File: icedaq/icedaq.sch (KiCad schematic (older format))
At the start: 14 parts, among them P1 UART, U1 REG12, U2 iCE40HX1K-VQ100, U3 RPi

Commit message: icedaq: update
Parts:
- added unit 3 of U2
- added unit 6 of U2
- CR1, CR2: footprint (none) -> Capacitors_SMD:C_0603_HandSoldering
- D2_5: footprint (none) -> local:D_0603_HandSoldering
- P1: footprint (none) -> Pin_Headers:Pin_Header_Straight_1x04
- R121, R122, R123, RDN1, RRST1, RSCK1, RSS1: footprint (none) -> Resistors_SMD:R_0603_HandSoldering
- U1: footprint (none) -> local:SOT23-5
- U2: footprint (none) -> local:VQFP-100
- U3: footprint (none) -> Pin_Headers:Pin_Header_Straight_2x20
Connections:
- wire segments 53 -> 57
- no-connect marks 14 -> 55
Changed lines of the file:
@@
 LIBS:rpi
 LIBS:adc082s021
+LIBS:dacx311
 LIBS:icedaq-cache
 EELAYER 25 0
@@
 F 0 "U1" H 9050 1700 60  0000 C CNN
 F 1 "REG12" H 8850 1350 60  0001 C CNN
-F 2 "" H 8850 1450 60  0000 C CNN
+F 2 "local:SOT23-5" H 8850 1450 60  0001 C CNN
 F 3 "" H 8850 1450 60  0000 C CNN
 	1    8850 1400
@@
 F 0 "CR1" H 8200 1350 50  0000 L CNN
 F 1 "1u" H 8110 1270 50  0000 L CNN
-F 2 "" H 8100 1350 50  0000 C CNN
+F 2 "Capacitors_SMD:C_0603_HandSoldering" H 8100 1350 50  0001 C CNN
 F 3 "" H 8100 1350 50  0000 C CNN
 	1    8100 1350
@@
 F 0 "CR2" H 10100 1350 50  0000 L CNN
 F 1 "1u" H 10010 1270 50  0000 L CNN
-F 2 "" H 10000 1350 50  0000 C CNN
+F 2 "Capacitors_SMD:C_0603_HandSoldering" H 10000 1350 50  0001 C CNN
 F 3 "" H 10000 1350 50  0000 C CNN
 	1    10000 1350
@@
 F 0 "R121" V 9580 1400 50  0000 C CNN
 F 1 "10k" V 9500 1400 50  0000 C CNN
-F 2 "" V 9430 1400 50  0000 C CNN
+F 2 "Resistors_SMD:R_0603_HandSoldering" V 9430 1400 50  0001 C CNN
 F 3 "" H 9500 1400 50  0000 C CNN
 	1    9500 1400
@@
 F 0 "R122" V 9830 1400 50  0000 C CNN
 F 1 "10k" V 9750 1400 50  0000 C CNN
-F 2 "" V 9680 1400 50  0000 C CNN
+F 2 "Resistors_SMD:R_0603_HandSoldering" V 9680 1400 50  0001 C CNN
 F 3 "" H 9750 1400 50  0000 C CNN
 	1    9750 1400
@@
 F 0 "R123" V 9830 1850 50  0000 C CNN
 F 1 "10k" V 9750 1850 50  0000 C CNN
-F 2 "" V 9680 1850 50  0000 C CNN
+F 2 "Resistors_SMD:R_0603_HandSoldering" V 9680 1850 50  0001 C CNN
 F 3 "" H 9750 1850 50  0000 C CNN
 	1    9750 1850
@@
 F 0 "U2" H 5900 2000 60  0000 C CNN
 F 1 "iCE40HX1K-VQ100" H 5850 2200 60  0001 C CNN
-F 2 "" H 6100 1500 60  0000 C CNN
+F 2 "local:VQFP-100" H 6100 1500 60  0001 C CNN
 F 3 "" H 6100 1500 60  0000 C CNN
 	1    5850 1400
@@
 F 0 "D2_5" H 6700 1730 50  0000 L CNN
 F 1 "D_Schottky_Small" H 6470 1570 50  0001 L CNN
-F 2 "" V 6750 1650 50  0000 C CNN
+F 2 "local:D_0603_HandSoldering" V 6750 1650 50  0001 C CNN
 F 3 "" V 6750 1650 50  0000 C CNN
 	1    6750 1650
@@
 F 0 "U2" H 3300 1650 60  0000 C CNN
 F 1 "iCE40HX1K-VQ100" H 3150 2150 60  0001 C CNN
-F 2 "" H 3400 1450 60  0000 C CNN
+F 2 "local:VQFP-100" H 3400 1450 60  0001 C CNN
 F 3 "" H 3400 1450 60  0000 C CNN
 	2    3150 1350
@@
 F 0 "RDN1" H 4350 1800 50  0000 C CNN
 F 1 "10k" V 4200 1800 50  0000 C CNN
-F 2 "" V 4130 1800 50  0000 C CNN
+F 2 "Resistors_SMD:R_0603_HandSoldering" V 4130 1800 50  0001 C CNN
 F 3 "" H 4200 1800 50  0000 C CNN
 	1    4200 1800
@@
 F 0 "RRST1" H 4000 1900 50  0000 C CNN
 F 1 "10k" V 3850 1900 50  0000 C CNN
-F 2 "" V 3780 1900 50  0000 C CNN
+F 2 "Resistors_SMD:R_0603_HandSoldering" V 3780 1900 50  0001 C CNN
 F 3 "" H 3850 1900 50  0000 C CNN
 	1    3850 1900
@@
 F 0 "RSCK1" H 4200 1300 50  0000 C CNN
 F 1 "10k" V 4000 1300 50  0000 C CNN
-F 2 "" V 3930 1300 50  0000 C CNN
+F 2 "Resistors_SMD:R_0603_HandSoldering" V 3930 1300 50  0001 C CNN
 F 3 "" H 4000 1300 50  0000 C CNN
 	1    4000 1300
@@
 F 0 "RSS1" H 4600 1400 50  0000 C CNN
 F 1 "10k" V 4400 1400 50  0000 C CNN
-F 2 "" V 4330 1400 50  0000 C CNN
+F 2 "Resistors_SMD:R_0603_HandSoldering" V 4330 1400 50  0001 C CNN
 F 3 "" H 4400 1400 50  0000 C CNN
 	1    4400 1400
@@
 F 0 "U3" H 9500 5800 60  0000 C CNN
 F 1 "RPi" H 8950 5050 60  0000 C CNN
-F 2 "" H 8750 4500 60  0000 C CNN
+F 2 "Pin_Headers:Pin_Header_Straight_2x20" H 8750 4500 60  0001 C CNN
 F 3 "" H 8750 4500 60  0000 C CNN
 	1    8750 4500
@@
 F 0 "P1" H 8800 3000 50  0000 C CNN
 F 1 "UART" V 8900 2750 50  0000 C CNN
-F 2 "" H 8800 2750 50  0000 C CNN
+F 2 "Pin_Headers:Pin_Header_Straight_1x04" H 8800 2750 50  0001 C CNN
 F 3 "" H 8800 2750 50  0000 C CNN
 	1    8800 2750
@@
 	3600 1350 3850 1350
 Wire Wire Line
-	3600 1450 4000 1450
-Wire Wire Line
-	3600 1550 4400 1550
-Wire Wire Line
-	3600 1650 4200 1650
-Wire Wire Line
-	3600 1750 3850 1750
+	3600 1450 4100 1450
+Wire Wire Line
+	3600 1550 4500 1550
+Wire Wire Line
+	3600 1650 4300 1650
+Wire Wire Line
+	3600 1750 3950 1750
 Wire Wire Line
 	9800 3650 9800 3750
@@
 F 0 "U2" H 5550 5300 60  0000 C CNN
 F 1 "iCE40HX1K-VQ100" H 5100 5500 60  0001 C CNN
-F 2 "" H 5350 4800 60  0000 C CNN
+F 2 "local:VQFP-100" H 5350 4800 60  0001 C CNN
 F 3 "" H 5350 4800 60  0000 C CNN
 	5    5100 4700
@@
 	4400 4900 4100 4900
 $Comp
-L +3.3V #PWR?
+L +3.3V #PWR025
 U 1 1 58615E10
 P 5450 5300
-F 0 "#PWR?" H 5450 5150 50  0001 C CNN
+F 0 "#PWR025" H 5450 5150 50  0001 C CNN
 F 1 "+3.3V" H 5450 5440 50  0000 C CNN
 F 2 "" H 5450 5300 50  0000 C CNN
@@
 Connection ~ 5350 5300
 $Sheet
-S 1200 3300 1200 1250
+S 1000 1100 1200 1250
 U 58616DAE
 F0 "Analog" 60
 F1 "icedaq-analog.sch" 60
 $EndSheet
+NoConn ~ 5750 4700
+NoConn ~ 4400 4700
+NoConn ~ 4400 4600
+NoConn ~ 4400 4500
+NoConn ~ 4400 4400
+$Comp
+L iCE40HX1K-VQ100 U2
+U 3 1 59912301
+P 2300 6350
+F 0 "U2" H 2750 6950 60  0000 C CNN
+F 1 "iCE40HX1K-VQ100" H 2300 7150 60  0001 C CNN
+F 2 "local:VQFP-100" H 2550 6450 60  0001 C CNN
+F 3 "" H 2550 6450 60  0000 C CNN
+	3    2300 6350
+	1    0    0    -1
+$EndComp
+$Comp
+L iCE40HX1K-VQ100 U2
+U 6 1 599123FB
+P 4350 6400
+F 0 "U2" H 4800 7000 60  0000 C CNN
+F 1 "iCE40HX1K-VQ100" H 4350 7200 60  0001 C CNN
+F 2 "local:VQFP-100" H 4600 6500 60  0001 C CNN
+F 3 "" H 4600 6500 60  0000 C CNN
+	6    4350 6400
+	1    0    0    -1
+$EndComp
+Connection ~ 4000 1450
+Connection ~ 4400 1550
+Connection ~ 4200 1650
+Connection ~ 3850 1750
+NoConn ~ 5300 6000
+NoConn ~ 5300 6100
+NoConn ~ 5300 6200
+NoConn ~ 5300 6300
+NoConn ~ 5300 6400
+NoConn ~ 5300 6500
+NoConn ~ 5300 6600
+NoConn ~ 5300 6700
+NoConn ~ 3600 6900
+NoConn ~ 3600 6800
+NoConn ~ 3600 6700
+NoConn ~ 3600 6600
+NoConn ~ 3600 6500
+NoConn ~ 3600 6400
+NoConn ~ 3600 6300
+NoConn ~ 3600 6200
+NoConn ~ 3600 6100
+NoConn ~ 3600 6000
+NoConn ~ 3050 6850
+NoConn ~ 3050 6750
+NoConn ~ 3050 6650
+NoConn ~ 3050 6550
+NoConn ~ 3050 6450
+NoConn ~ 3050 6350
+NoConn ~ 3050 6250
+NoConn ~ 3050 6150
+NoConn ~ 3050 6050
+NoConn ~ 1600 6050
+NoConn ~ 1600 6150
+NoConn ~ 1600 6250
+NoConn ~ 1600 6350
+NoConn ~ 1600 6450
+NoConn ~ 1600 6550
+NoConn ~ 1600 6650
+NoConn ~ 1600 6750
+NoConn ~ 1600 6850
+Wire Wire Line
+	2350 7200 2450 7200
+Wire Wire Line
+	2450 7200 2450 7250
+Wire Wire Line
+	4600 7300 4700 7300
+Wire Wire Line
+	4700 7300 4700 7350
+$Comp
+L +3.3V #PWR026
+U 1 1 59914C50
+P 4700 7350
+F 0 "#PWR026" H 4700 7200 50  0001 C CNN
+F 1 "+3.3V" H 4700 7490 50  0000 C CNN
+F 2 "" H 4700 7350 50  0000 C CNN
+F 3 "" H 4700 7350 50  0000 C CNN
+	1    4700 7350
+	-1   0    0    1
+$EndComp
+$Comp
+L +3.3V #PWR027
+U 1 1 59914C91
+P 2450 7250
+F 0 "#PWR027" H 2450 7100 50  0001 C CNN
+F 1 "+3.3V" H 2450 7390 50  0000 C CNN
+F 2 "" H 2450 7250 50  0000 C CNN
+F 3 "" H 2450 7250 50  0000 C CNN
+	1    2450 7250
+	-1   0    0    1
+$EndComp
 $EndSCHEMATC

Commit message: icedaq layout
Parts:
- removed unit 3 of U2
- added CD1, CD3, CD4, CD5: C_Small, Capacitors_SMD:C_0603_HandSoldering, symbol C_Small
- added R1: 10k, Resistors_SMD:R_0603_HandSoldering, symbol R
- added RB1, RB2: 3.9k, Resistors_SMD:R_0603_HandSoldering, symbol R
- added ROM1: CAT24C, Housings_SOIC:SOIC-8_3.9x4.9mm_Pitch1.27mm, symbol 24LC32
- added U4: oscillator4, local:OSC_SMD_1, symbol oscillator4
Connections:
- net labels added: ID_SC, ID_SD, clk
- wire segments 57 -> 67
- no-connect marks 55 -> 37
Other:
- note added: "Break out MCU UART"
- note added: "See https://github.com/raspberrypi/hats/blob/master/designguide.md"
- note added: "UART"
- note added: "Write protect\nflows low (disabled)"
- note removed: "UART to\nheader"
- moved on the sheet: P1

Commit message: icedaq more
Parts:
- added P2: GPIO, Pin_Headers:Pin_Header_Straight_1x05_Pitch2.00mm, symbol CONN_01X05
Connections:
- wire segments 67 -> 71
- no-connect marks 37 -> 33
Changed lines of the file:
@@
 NoConn ~ 5300 6200
 NoConn ~ 5300 6300
-NoConn ~ 5300 6400
-NoConn ~ 5300 6500
-NoConn ~ 5300 6600
-NoConn ~ 5300 6700
 NoConn ~ 3600 6800
 NoConn ~ 3600 6700
@@
 $EndComp
 $Comp
-L GND #PWR031
+L GND #PWR029
 U 1 1 599273C4
 P 4150 3100
-F 0 "#PWR031" H 4150 2850 50  0001 C CNN
+F 0 "#PWR029" H 4150 2850 50  0001 C CNN
 F 1 "GND" H 4150 2950 50  0000 C CNN
 F 2 "" H 4150 3100 50  0000 C CNN
@@
 $EndComp
 $Comp
-L +3.3V #PWR032
+L +3.3V #PWR030
 U 1 1 599273CA
 P 4150 2900
-F 0 "#PWR032" H 4150 2750 50  0001 C CNN
+F 0 "#PWR030" H 4150 2750 50  0001 C CNN
 F 1 "+3.3V" H 4150 3040 50  0000 C CNN
 F 2 "" H 4150 2900 50  0000 C CNN
@@
 $EndComp
 $Comp
-L GND #PWR033
+L GND #PWR031
 U 1 1 599274AA
 P 3400 3100
-F 0 "#PWR033" H 3400 2850 50  0001 C CNN
+F 0 "#PWR031" H 3400 2850 50  0001 C CNN
 F 1 "GND" H 3400 2950 50  0000 C CNN
 F 2 "" H 3400 3100 50  0000 C CNN
@@
 $EndComp
 $Comp
-L +3.3V #PWR034
+L +3.3V #PWR032
 U 1 1 599274B0
 P 3400 2900
-F 0 "#PWR034" H 3400 2750 50  0001 C CNN
+F 0 "#PWR032" H 3400 2750 50  0001 C CNN
 F 1 "+3.3V" H 3400 3040 50  0000 C CNN
 F 2 "" H 3400 2900 50  0000 C CNN
@@
 $EndComp
 $Comp
-L GND #PWR035
+L GND #PWR033
 U 1 1 59927E27
 P 6400 2850
-F 0 "#PWR035" H 6400 2600 50  0001 C CNN
+F 0 "#PWR033" H 6400 2600 50  0001 C CNN
 F 1 "GND" H 6400 2700 50  0000 C CNN
 F 2 "" H 6400 2850 50  0000 C CNN
@@
 $EndComp
 $Comp
-L +1V2 #PWR036
+L +1V2 #PWR034
 U 1 1 59927E92
 P 6400 2650
-F 0 "#PWR036" H 6400 2500 50  0001 C CNN
+F 0 "#PWR034" H 6400 2500 50  0001 C CNN
 F 1 "+1V2" H 6400 2790 50  0000 C CNN
 F 2 "" H 6400 2650 50  0000 C CNN
@@
 $EndComp
 $Comp
-L GND #PWR037
+L GND #PWR035
 U 1 1 59927F5C
 P 6650 2850
-F 0 "#PWR037" H 6650 2600 50  0001 C CNN
+F 0 "#PWR035" H 6650 2600 50  0001 C CNN
 F 1 "GND" H 6650 2700 50  0000 C CNN
 F 2 "" H 6650 2850 50  0000 C CNN
@@
 $EndComp
 $Comp
-L +1V2 #PWR038
+L +1V2 #PWR036
 U 1 1 59927F62
 P 6650 2650
-F 0 "#PWR038" H 6650 2500 50  0001 C CNN
+F 0 "#PWR036" H 6650 2500 50  0001 C CNN
 F 1 "+1V2" H 6650 2790 50  0000 C CNN
 F 2 "" H 6650 2650 50  0000 C CNN
@@
 F 1 "CAT24C" H 1750 6550 50  0000 C CNN
 F 2 "Housings_SOIC:SOIC-8_3.9x4.9mm_Pitch1.27mm" H 1600 6050 50  0001 L CNN
-F 3 "" H 1550 6200 50  0000 C CNN
+F 3 "http://www.onsemi.com/pub/Collateral/CAT24C32-D.PDF" H 1550 6200 50  0001 C CNN
 	1    1550 6300
 	1    0    0    -1
 $EndComp
 $Comp
-L GND #PWR039
+L GND #PWR037
 U 1 1 5992C4A3
 P 1550 6600
-F 0 "#PWR039" H 1550 6350 50  0001 C CNN
+F 0 "#PWR037" H 1550 6350 50  0001 C CNN
 F 1 "GND" H 1550 6450 50  0000 C CNN
 F 2 "" H 1550 6600 50  0000 C CNN
@@
 Connection ~ 1150 6400
 $Comp
-L GND #PWR040
+L GND #PWR038
 U 1 1 5992C6A3
 P 1150 6550
-F 0 "#PWR040" H 1150 6300 50  0001 C CNN
+F 0 "#PWR038" H 1150 6300 50  0001 C CNN
 F 1 "GND" H 1150 6400 50  0000 C CNN
 F 2 "" H 1150 6550 50  0000 C CNN
@@
 $EndComp
 $Comp
-L +3.3V #PWR041
+L +3.3V #PWR039
 U 1 1 5992C712
 P 1550 6000
-F 0 "#PWR041" H 1550 5850 50  0001 C CNN
+F 0 "#PWR039" H 1550 5850 50  0001 C CNN
 F 1 "+3.3V" H 1550 6140 50  0000 C CNN
 F 2 "" H 1550 6000 50  0000 C CNN
@@
 $EndComp
 $Comp
-L +3.3V #PWR042
+L +3.3V #PWR040
 U 1 1 5992D326
 P 2200 5750
-F 0 "#PWR042" H 2200 5600 50  0001 C CNN
+F 0 "#PWR040" H 2200 5600 50  0001 C CNN
 F 1 "+3.3V" H 2200 5890 50  0000 C CNN
 F 2 "" H 2200 5750 50  0000 C CNN
@@
 $EndComp
 $Comp
-L +3.3V #PWR043
+L +3.3V #PWR041
 U 1 1 5992D39D
 P 2450 5750
-F 0 "#PWR043" H 2450 5600 50  0001 C CNN
+F 0 "#PWR041" H 2450 5600 50  0001 C CNN
 F 1 "+3.3V" H 2450 5890 50  0000 C CNN
 F 2 "" H 2450 5750 50  0000 C CNN
@@
 	9800 3500 9950 3500
 NoConn ~ 1950 6400
+$Comp
+L CONN_01X05 P2
+U 1 1 59932164
+P 5700 6600
+F 0 "P2" H 5700 6900 50  0000 C CNN
+F 1 "GPIO" V 5800 6600 50  0000 C CNN
+F 2 "Pin_Headers:Pin_Header_Straight_1x05_Pitch2.00mm" H 5700 6600 50  0001 C CNN
+F 3 "" H 5700 6600 50  0000 C CNN
+	1    5700 6600
+	1    0    0    -1
+$EndComp
+Wire Wire Line
+	5500 6400 5300 6400
+Wire Wire Line
+	5300 6500 5500 6500
+Wire Wire Line
+	5500 6600 5300 6600
+Wire Wire Line
+	5300 6700 5500 6700
+$Comp
+L GND #PWR042
+U 1 1 599324BC
+P 5500 6800
+F 0 "#PWR042" H 5500 6550 50  0001 C CNN
+F 1 "GND" H 5500 6650 50  0000 C CNN
+F 2 "" H 5500 6800 50  0000 C CNN
+F 3 "" H 5500 6800 50  0000 C CNN
+	1    5500 6800
+	1    0    0    -1
+$EndComp
 $EndSCHEMATC

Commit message: minor
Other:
- note added: "Identification EEPROM"
- note added: "iCE40 configure control\n(GPIO)"
- note removed: "iCE40 configure control"
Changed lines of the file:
@@
 SPI1 for debug
 Text Notes 7400 5650 2    60   ~ 0
-iCE40 configure control
+iCE40 configure control\n(GPIO)
 Text Notes 7350 4650 2    60   ~ 0
 UART
@@
 	1    0    0    -1
 $EndComp
+Text Notes 800  5650 0    60   ~ 0
+Identification EEPROM
 $EndSCHEMATC

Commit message: icedaq: update
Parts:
- added TP1: WP, local:testpoint, symbol TEST
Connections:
- net labels removed: GCLK2
- wire segments 71 -> 66
- no-connect marks 33 -> 37
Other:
- note added: "SPI0 for application"
- note added: "SPI1 for configure/debug"
- note added: "https://github.com/raspberrypi/hats/blob/master/designguide.md"
- note removed: "SPI0 to configure"
- note removed: "SPI1 for debug"
- note removed: "See https://github.com/raspberrypi/hats/blob/master/designguide.md"
- moved on the sheet: P2
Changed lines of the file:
@@
 Title "iCE40 Raspberry Pi 3b GPIO"
 Date ""
-Rev "1"
+Rev "draft"
 Comp "MAD"
 Comment1 ""
@@
 	1    0    0    -1
 $EndComp
-Text Label 7800 4100 2    60   ~ 0
+Text Label 7800 5100 2    60   ~ 0
 MISO
-Text Label 7800 4200 2    60   ~ 0
+Text Label 7800 5200 2    60   ~ 0
 MOSI
-Text Label 7800 4300 2    60   ~ 0
+Text Label 7800 5300 2    60   ~ 0
 SCK
-Text Label 7750 4000 2    60   ~ 0
+Text Label 7750 4800 2    60   ~ 0
 SS
 Text Label 7800 5600 2    60   ~ 0
@@
 NoConn ~ 7850 5400
 NoConn ~ 7850 4900
-NoConn ~ 7850 4800
+NoConn ~ 7850 5000
 NoConn ~ 7850 3900
 NoConn ~ 7850 3500
@@
 Text Label 7800 4700 2    60   ~ 0
 RXD
-Text Label 7800 5000 2    60   ~ 0
-SS1
-Text Label 7800 5100 2    60   ~ 0
-MISO1
-Text Label 7800 5200 2    60   ~ 0
-MOSI1
-Text Label 7800 5300 2    60   ~ 0
-SCLK1
-Text Notes 7350 4150 2    60   ~ 0
-SPI0 to configure
+Text Notes 7100 4150 2    60   ~ 0
+SPI0 for application
 Text Notes 7350 5150 2    60   ~ 0
-SPI1 for debug
+SPI1 for configure/debug
 Text Notes 7400 5650 2    60   ~ 0
 iCE40 configure control\n(GPIO)
@@
 Connection ~ 9800 4250
 Wire Wire Line
-	7850 4100 7600 4100
-Wire Wire Line
-	7850 4200 7600 4200
-Wire Wire Line
-	7850 4300 7600 4300
-Wire Wire Line
-	7850 4000 7600 4000
+	7850 5100 7600 5100
+Wire Wire Line
+	7850 5200 7600 5200
+Wire Wire Line
+	7850 5300 7600 5300
+Wire Wire Line
+	7850 4800 7600 4800
 Wire Wire Line
 	7850 5700 7600 5700
@@
 Connection ~ 6550 1650
 Wire Wire Line
-	7850 3600 7650 3600
-Wire Wire Line
 	7850 3700 7650 3700
 Wire Wire Line
@@
 	7850 4700 7600 4700
 Wire Wire Line
-	7850 5000 7600 5000
-Wire Wire Line
-	7850 5100 7600 5100
-Wire Wire Line
-	7850 5200 7600 5200
-Wire Wire Line
-	7850 5300 7600 5300
+	7850 4000 7750 4000
+Wire Wire Line
+	7850 4100 7450 4100
+Wire Wire Line
+	7850 4200 7800 4200
+Wire Wire Line
+	7850 4300 7450 4300
 Wire Wire Line
 	6900 6100 6650 6100
@@
 Text Label 4300 5000 2    60   ~ 0
 GCLK1
-Wire Wire Line
-	5750 4300 6050 4300
-Wire Wire Line
-	5750 4400 6050 4400
-Wire Wire Line
-	5750 4500 6050 4500
-Wire Wire Line
-	5750 4600 6050 4600
-Text Label 5850 4300 0    60   ~ 0
-SS1
-Text Label 5800 4600 0    60   ~ 0
-MISO1
-Text Label 5800 4500 0    60   ~ 0
-MOSI1
-Text Label 5800 4400 0    60   ~ 0
-SCLK1
 Wire Wire Line
 	4400 4900 4100 4900
@@
 NoConn ~ 5300 6300
 NoConn ~ 3600 6800
-NoConn ~ 3600 6700
-NoConn ~ 3600 6600
-NoConn ~ 3600 6500
-NoConn ~ 3600 6400
 NoConn ~ 3600 6300
 NoConn ~ 3600 6200
@@
 	1    0    0    -1
 $EndComp
-Text GLabel 2950 4000 2    60   Input ~ 0
+Text GLabel 2950 4000 2    60   Output ~ 0
 clk
 $Comp
@@
 $EndComp
 NoConn ~ 4400 4800
-Text GLabel 7650 3550 1    60   Input ~ 0
-GCLK2
-Wire Wire Line
-	7650 3600 7650 3550
-Text Notes 6350 6900 0    60   ~ 0
-See https://github.com/raspberrypi/hats/blob/master/designguide.md
+Text Notes 7200 3050 0    60   ~ 0
+https://github.com/raspberrypi/hats/blob/master/designguide.md
 Text Notes 7300 6450 0    60   ~ 0
 Break out MCU UART
@@
 	1    0    0    -1
 $EndComp
-Text Notes 1800 6850 0    60   ~ 0
+Text Notes 1700 7150 0    60   ~ 0
 Write protect\nflows low (disabled)
 $Comp
@@
 Wire Wire Line
 	9800 3500 9950 3500
-NoConn ~ 1950 6400
 $Comp
 L CONN_01X05 P2
 U 1 1 59932164
-P 5700 6600
-F 0 "P2" H 5700 6900 50  0000 C CNN
-F 1 "GPIO" V 5800 6600 50  0000 C CNN
-F 2 "Pin_Headers:Pin_Header_Straight_1x05_Pitch2.00mm" H 5700 6600 50  0001 C CNN
-F 3 "" H 5700 6600 50  0000 C CNN
-	1    5700 6600
-	1    0    0    -1
-$EndComp
-Wire Wire Line
-	5500 6400 5300 6400
-Wire Wire Line
-	5300 6500 5500 6500
-Wire Wire Line
-	5500 6600 5300 6600
-Wire Wire Line
-	5300 6700 5500 6700
+P 3200 6600
+F 0 "P2" H 3200 6900 50  0000 C CNN
+F 1 "GPIO" V 3300 6600 50  0000 C CNN
+F 2 "Pin_Headers:Pin_Header_Straight_1x05_Pitch2.00mm" H 3200 6600 50  0001 C CNN
+F 3 "" H 3200 6600 50  0000 C CNN
+	1    3200 6600
+	-1   0    0    -1
+$EndComp
+Wire Wire Line
+	3400 6400 3600 6400
+Wire Wire Line
+	3600 6500 3400 6500
+Wire Wire Line
+	3400 6600 3600 6600
+Wire Wire Line
+	3600 6700 3400 6700
 $Comp
 L GND #PWR042
 U 1 1 599324BC
-P 5500 6800
-F 0 "#PWR042" H 5500 6550 50  0001 C CNN
-F 1 "GND" H 5500 6650 50  0000 C CNN
-F 2 "" H 5500 6800 50  0000 C CNN
-F 3 "" H 5500 6800 50  0000 C CNN
-	1    5500 6800
-	1    0    0    -1
+P 3400 6800
+F 0 "#PWR042" H 3400 6550 50  0001 C CNN
+F 1 "GND" H 3400 6650 50  0000 C CNN
+F 2 "" H 3400 6800 50  0000 C CNN
+F 3 "" H 3400 6800 50  0000 C CNN
+	1    3400 6800
+	-1   0    0    -1
 $EndComp
 Text Notes 800  5650 0    60   ~ 0
 Identification EEPROM
+Text GLabel 7750 4000 0    60   Output ~ 0
+SS1
+Text GLabel 7450 4100 0    60   Input ~ 0
+MISO1
+Text GLabel 7800 4200 0    60   Output ~ 0
+MOSI1
+Text GLabel 7450 4300 0    60   Output ~ 0
+SCLK1
+NoConn ~ 5750 4300
+NoConn ~ 5750 4400
+NoConn ~ 5750 4500
+NoConn ~ 5750 4600
+NoConn ~ 5300 6400
+NoConn ~ 5300 6500
+NoConn ~ 5300 6600
+NoConn ~ 5300 6700
+NoConn ~ 7850 3600
+$Comp
+L TEST TP1
+U 1 1 599CB445
+P 2100 6400
+F 0 "TP1" H 2100 6700 50  0000 C BNN
+F 1 "WP" H 2100 6650 50  0000 C CNN
+F 2 "local:testpoint" H 2100 6400 50  0001 C CNN
+F 3 "" H 2100 6400 50  0000 C CNN
+	1    2100 6400
+	-1   0    0    1
+$EndComp
+Wire Wire Line
+	2100 6400 1950 6400
 $EndSCHEMATC

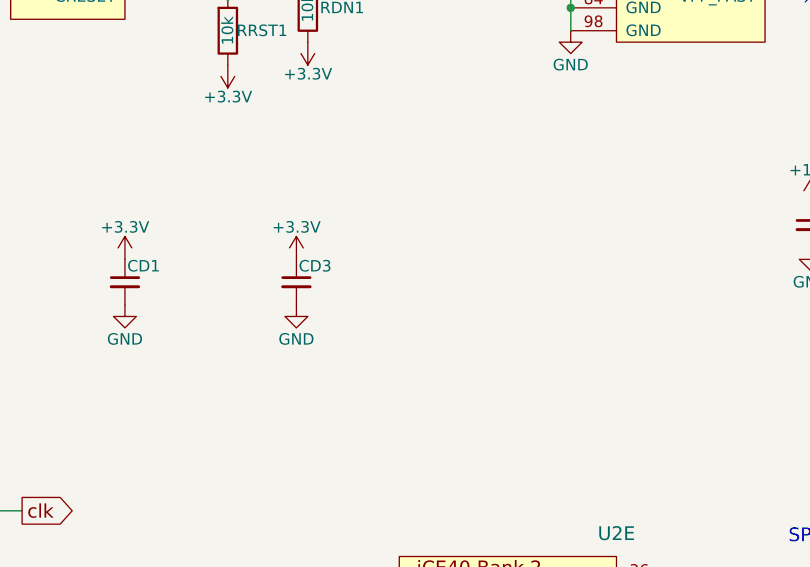
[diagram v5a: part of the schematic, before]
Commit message: icedaq: layout take 2
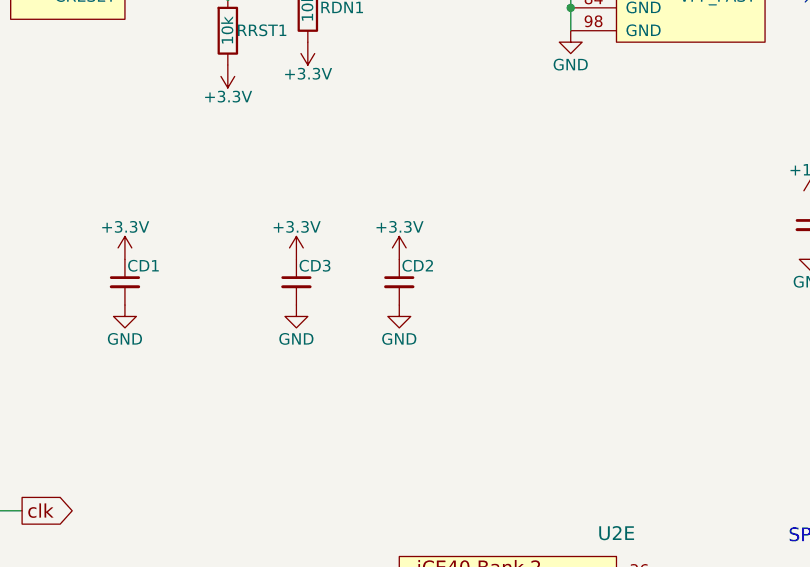
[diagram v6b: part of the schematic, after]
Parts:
- added CD2: C_Small, Capacitors_SMD:C_0603_HandSoldering, symbol C_Small

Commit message: icedaq: relocate connectors
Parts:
- added P3: GPIO2, local:gpio, symbol CONN_01X04
- added P4: GPIO3, local:gpio, symbol CONN_01X04
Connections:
- wire segments 66 -> 74
- no-connect marks 37 -> 29
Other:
- note added: "1.2V regulator for FPGA core\ninput from 3.3V\n"
- note removed: "1.2V regulator for FPGA core\ninput from 3.3V or 5V\n"
- moved on the sheet: P2
